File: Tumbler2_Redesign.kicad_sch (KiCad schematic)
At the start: 4 parts

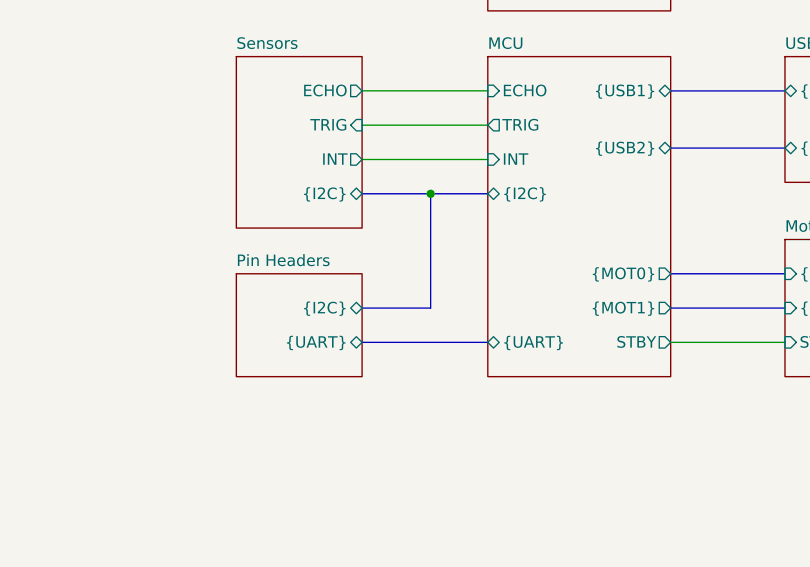
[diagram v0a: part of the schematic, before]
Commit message: Add expansion pin headers
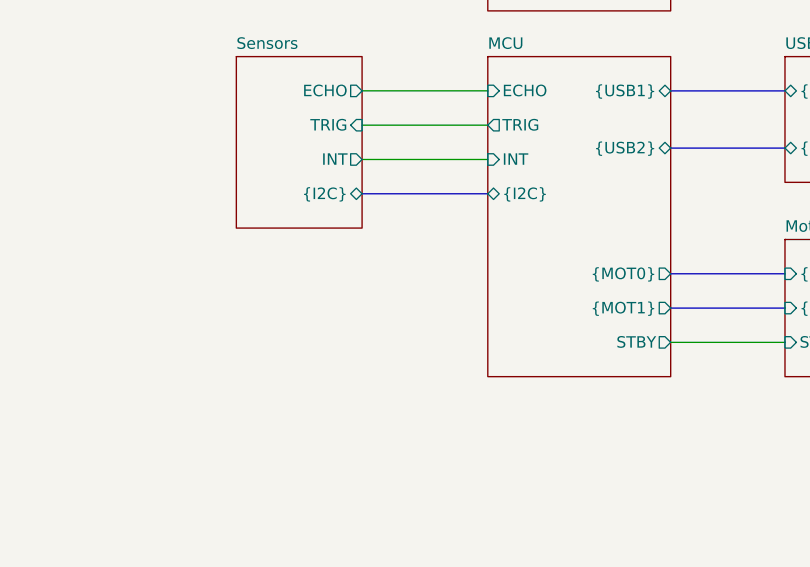
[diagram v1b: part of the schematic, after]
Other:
- removed sheet Pin Headers
- sheet MCU ports: added none; removed {UART}
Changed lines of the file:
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@@
 		)
-	)
-	(junction
-		(at 127 99.06)
-		(diameter 0)
-		(color 0 0 0 0)
 	)
 	(wire
@@
 	(bus
 		(pts
-			(xy 119.38 115.57) (xy 133.35 115.57)
+			(xy 153.67 87.63) (xy 166.37 87.63)
 		)
 		(stroke
@@
 	(bus
 		(pts
-			(xy 153.67 87.63) (xy 166.37 87.63)
+			(xy 153.67 111.76) (xy 166.37 111.76)
+		)
+		(stroke
+			(width 0)
+			(type default)
+		)
+	)
+	(wire
+		(pts
+			(xy 119.38 91.44) (xy 133.35 91.44)
 		)
 		(stroke
@@
 	(bus
 		(pts
-			(xy 153.67 111.76) (xy 166.37 111.76)
+			(xy 153.67 107.95) (xy 166.37 107.95)
 		)
 		(stroke
@@
 	(wire
 		(pts
-			(xy 119.38 91.44) (xy 133.35 91.44)
+			(xy 119.38 95.25) (xy 133.35 95.25)
 		)
 		(stroke
@@
 	(bus
 		(pts
-			(xy 153.67 107.95) (xy 166.37 107.95)
+			(xy 153.67 93.98) (xy 166.37 93.98)
+		)
+		(stroke
+			(width 0)
+			(type default)
+		)
+	)
+	(wire
+		(pts
+			(xy 153.67 115.57) (xy 166.37 115.57)
 		)
 		(stroke
@@
 	(bus
 		(pts
-			(xy 127 99.06) (xy 133.35 99.06)
-		)
-		(stroke
-			(width 0)
-			(type default)
-		)
-	)
-	(wire
-		(pts
-			(xy 119.38 95.25) (xy 133.35 95.25)
-		)
-		(stroke
-			(width 0)
-			(type default)
-		)
-	)
-	(bus
-		(pts
-			(xy 153.67 93.98) (xy 166.37 93.98)
-		)
-		(stroke
-			(width 0)
-			(type default)
-		)
-	)
-	(wire
-		(pts
-			(xy 153.67 115.57) (xy 166.37 115.57)
-		)
-		(stroke
-			(width 0)
-			(type default)
-		)
-	)
-	(bus
-		(pts
-			(xy 119.38 111.76) (xy 127 111.76)
-		)
-		(stroke
-			(width 0)
-			(type default)
-		)
-	)
-	(bus
-		(pts
-			(xy 119.38 99.06) (xy 127 99.06)
-		)
-		(stroke
-			(width 0)
-			(type default)
-		)
-	)
-	(bus
-		(pts
-			(xy 127 111.76) (xy 127 99.06)
+			(xy 119.38 99.06) (xy 133.35 99.06)
 		)
 		(stroke
@@
 			)
 		)
-		(pin "{UART}" bidirectional
-			(at 133.35 115.57 180)
-			(effects
-				(font
-					(size 1.27 1.27)
-				)
-				(justify left)
-			)
-		)
 		(instances
 			(project "Tumbler2_Redesign"
@@
 				)
 			)
-		)
-	)
-	(sheet
-		(at 105.41 107.95)
-		(size 13.97 11.43)
-		(exclude_from_sim no)
-		(in_bom yes)
-		(on_board yes)
-		(dnp no)
-		(fields_autoplaced yes)
-		(stroke
-			(width 0.1524)
-			(type solid)
-		)
-		(fill
-			(color 0 0 0 0.0000)
-		)
-		(property "Sheetname" "Pin Headers"
-			(at 105.41 107.2384 0)
-			(effects
-				(font
-					(size 1.27 1.27)
-				)
-				(justify left bottom)
-			)
-		)
-		(property "Sheetfile" "pin_headers.kicad_sch"
-			(at 105.41 119.9646 0)
-			(effects
-				(font
-					(size 1.27 1.27)
-				)
-				(justify left top)
-				(hide yes)
-			)
-		)
-		(pin "{I2C}" bidirectional
-			(at 119.38 111.76 0)
-			(effects
-				(font
-					(size 1.27 1.27)
-				)
-				(justify right)
-			)
-		)
-		(pin "{UART}" bidirectional
-			(at 119.38 115.57 0)
-			(effects
-				(font
-					(size 1.27 1.27)
-				)
-				(justify right)
-			)
-		)
-		(instances
-			(project "Tumbler2_Redesign"
-				(path "/f3fd8d79-9d35-4c04-811e-2697a2740958"
-					(page "7")
-				)
-			)

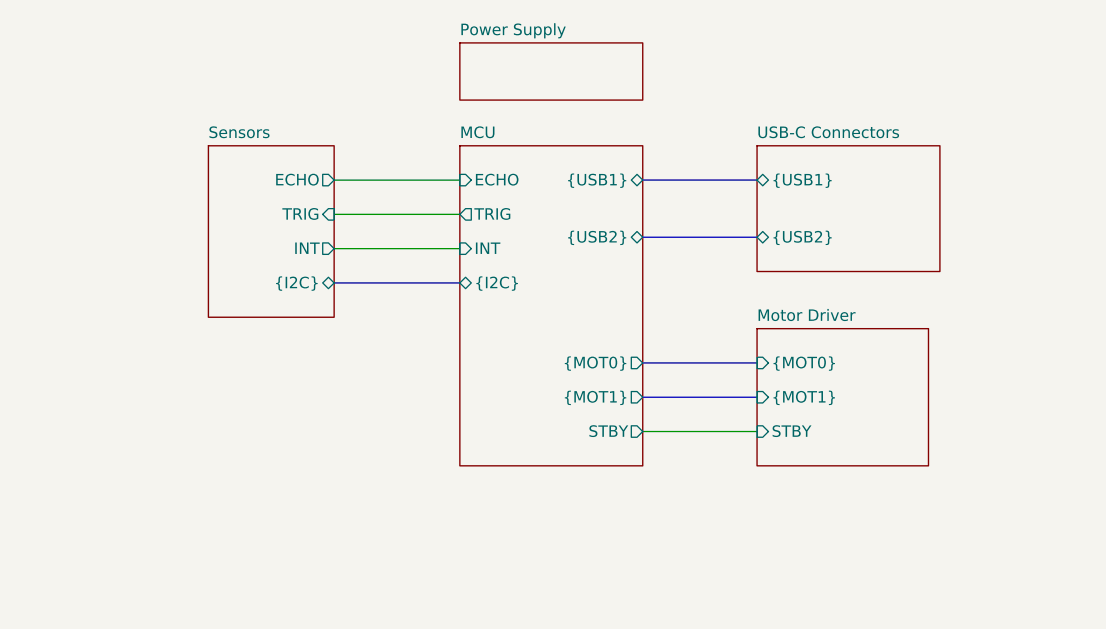
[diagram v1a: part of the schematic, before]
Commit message: Combine peripheral modules
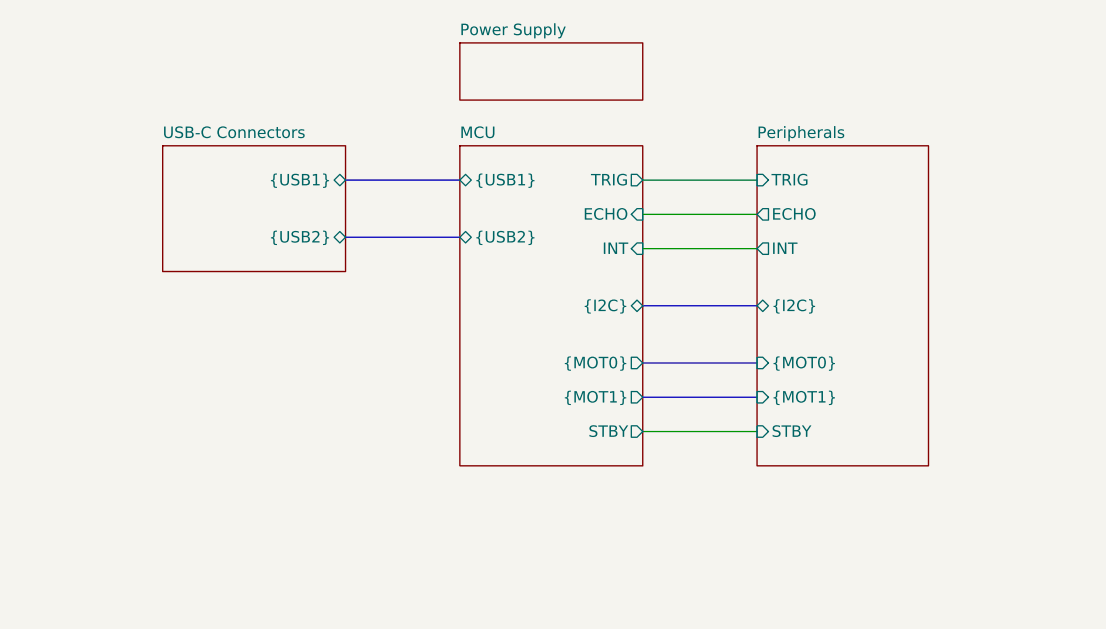
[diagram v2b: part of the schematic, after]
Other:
- removed sheet Motor Driver
- removed sheet Sensors
- added sheet Peripherals (peripherals.kicad_sch)
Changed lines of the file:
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@@
-		)
-	)
-	(wire
-		(pts
-			(xy 119.38 87.63) (xy 133.35 87.63)
-		)
-		(stroke
-			(width 0)
-			(type default)
-		)
-	)
-	(bus
-		(pts
-			(xy 153.67 87.63) (xy 166.37 87.63)
-		)
-		(stroke
-			(width 0)
-			(type default)
 		)
 	)
@@
 	(wire
 		(pts
-			(xy 119.38 91.44) (xy 133.35 91.44)
+			(xy 153.67 87.63) (xy 166.37 87.63)
 		)
 		(stroke
@@
 	(wire
 		(pts
-			(xy 119.38 95.25) (xy 133.35 95.25)
-		)
-		(stroke
-			(width 0)
-			(type default)
-		)
-	)
-	(bus
-		(pts
-			(xy 153.67 93.98) (xy 166.37 93.98)
+			(xy 153.67 95.25) (xy 166.37 95.25)
 		)
 		(stroke
@@
 		)
 	)
+	(wire
+		(pts
+			(xy 153.67 91.44) (xy 166.37 91.44)
+		)
+		(stroke
+			(width 0)
+			(type default)
+		)
+	)
 	(bus
 		(pts
-			(xy 119.38 99.06) (xy 133.35 99.06)
+			(xy 153.67 101.6) (xy 166.37 101.6)
+		)
+		(stroke
+			(width 0)
+			(type default)
+		)
+	)
+	(bus
+		(pts
+			(xy 120.65 93.98) (xy 133.35 93.98)
+		)
+		(stroke
+			(width 0)
+			(type default)
+		)
+	)
+	(bus
+		(pts
+			(xy 120.65 87.63) (xy 133.35 87.63)
 		)
 		(stroke
@@
 			)
 		)
+		(pin "{USB1}" bidirectional
+			(at 133.35 87.63 180)
+			(effects
+				(font
+					(size 1.27 1.27)
+				)
+				(justify left)
+			)
+		)
+		(pin "{USB2}" bidirectional
+			(at 133.35 93.98 180)
+			(effects
+				(font
+					(size 1.27 1.27)
+				)
+				(justify left)
+			)
+		)
 		(pin "ECHO" input
-			(at 133.35 87.63 180)
-			(effects
-				(font
-					(size 1.27 1.27)
-				)
-				(justify left)
+			(at 153.67 91.44 0)
+			(effects
+				(font
+					(size 1.27 1.27)
+				)
+				(justify right)
 			)
 		)
 		(pin "INT" input
-			(at 133.35 95.25 180)
-			(effects
-				(font
-					(size 1.27 1.27)
-				)
-				(justify left)
+			(at 153.67 95.25 0)
+			(effects
+				(font
+					(size 1.27 1.27)
+				)
+				(justify right)
 			)
 		)
 		(pin "TRIG" output
-			(at 133.35 91.44 180)
-			(effects
-				(font
-					(size 1.27 1.27)
-				)
-				(justify left)
-			)
-		)
-		(pin "{USB1}" bidirectional
 			(at 153.67 87.63 0)
 			(effects
@@
 			)
 		)
-		(pin "{USB2}" bidirectional
-			(at 153.67 93.98 0)
+		(pin "{I2C}" bidirectional
+			(at 153.67 101.6 0)
 			(effects
 				(font
@@
 			)
 		)
-		(pin "{I2C}" bidirectional
-			(at 133.35 99.06 180)
-			(effects
-				(font
-					(size 1.27 1.27)
-				)
-				(justify left)
-			)
-		)
 		(instances
 			(project "Tumbler2_Redesign"
@@
 	)
 	(sheet
-		(at 105.41 83.82)
-		(size 13.97 19.05)
+		(at 100.33 83.82)
+		(size 20.32 13.97)
 		(exclude_from_sim no)
 		(in_bom yes)
@@
 			(color 0 0 0 0.0000)
 		)
-		(property "Sheetname" "Sensors"
-			(at 105.41 83.1084 0)
+		(property "Sheetname" "USB-C Connectors"
+			(at 100.33 83.1084 0)
 			(effects
 				(font
@@
 			)
 		)
-		(property "Sheetfile" "sensors.kicad_sch"
-			(at 105.41 103.4546 0)
+		(property "Sheetfile" "usb_c_connector.kicad_sch"
+			(at 100.33 98.3746 0)
 			(effects
 				(font
@@
 			)
 		)
-		(pin "ECHO" output
-			(at 119.38 87.63 0)
+		(pin "{USB1}" bidirectional
+			(at 120.65 87.63 0)
 			(effects
 				(font
@@
 			)
 		)
-		(pin "INT" output
-			(at 119.38 95.25 0)
+		(pin "{USB2}" bidirectional
+			(at 120.65 93.98 0)
 			(effects
 				(font
@@
 			)
 		)
-		(pin "TRIG" input
-			(at 119.38 91.44 0)
-			(effects
-				(font
-					(size 1.27 1.27)
-				)
-				(justify right)
-			)
-		)
-		(pin "{I2C}" bidirectional
-			(at 119.38 99.06 0)
-			(effects
-				(font
-					(size 1.27 1.27)
-				)
-				(justify right)
-			)
-		)
 		(instances
 			(project "Tumbler2_Redesign"
 				(path "/f3fd8d79-9d35-4c04-811e-2697a2740958"
-					(page "5")
+					(page "4")
 				)
 			)
@@
 	(sheet
 		(at 166.37 83.82)
-		(size 20.32 13.97)
+		(size 19.05 35.56)
 		(exclude_from_sim no)
 		(in_bom yes)
@@
 			(color 0 0 0 0.0000)
 		)
-		(property "Sheetname" "USB-C Connectors"
+		(property "Sheetname" "Peripherals"
 			(at 166.37 83.1084 0)
 			(effects
@@
 			)
 		)
-		(property "Sheetfile" "usb_c_connector.kicad_sch"
-			(at 166.37 98.3746 0)
+		(property "Sheetfile" "peripherals.kicad_sch"
+			(at 166.37 119.9646 0)
 			(effects
 				(font
@@
 			)
 		)
-		(pin "{USB1}" bidirectional
+		(pin "ECHO" output
+			(at 166.37 91.44 180)
+			(effects
+				(font
+					(size 1.27 1.27)
+				)
+				(justify left)
+			)
+		)
+		(pin "INT" output
+			(at 166.37 95.25 180)
+			(effects
+				(font
+					(size 1.27 1.27)
+				)
+				(justify left)
+			)
+		)
+		(pin "STBY" input
+			(at 166.37 115.57 180)
+			(effects
+				(font
+					(size 1.27 1.27)
+				)
+				(justify left)
+			)
+		)
+		(pin "TRIG" input
 			(at 166.37 87.63 180)
 			(effects
@@
 			)
 		)
-		(pin "{USB2}" bidirectional
-			(at 166.37 93.98 180)
-			(effects
-				(font
-					(size 1.27 1.27)
-				)
-				(justify left)
-			)
-		)
-		(instances
-			(project "Tumbler2_Redesign"
-				(path "/f3fd8d79-9d35-4c04-811e-2697a2740958"
-					(page "4")
-				)
-			)
-		)
-	)
-	(sheet
-		(at 166.37 104.14)
-		(size 19.05 15.24)
-		(exclude_from_sim no)
-		(in_bom yes)
-		(on_board yes)
-		(dnp no)
-		(fields_autoplaced yes)
-		(stroke
-			(width 0.1524)
-			(type solid)
-		)
-		(fill
-			(color 0 0 0 0.0000)
-		)
-		(property "Sheetname" "Motor Driver"
-			(at 166.37 103.4284 0)
-			(effects
-				(font
-					(size 1.27 1.27)
-				)
-				(justify left bottom)
-			)
-		)
-		(property "Sheetfile" "motor_driver.kicad_sch"
-			(at 166.37 119.9646 0)
-			(effects
-				(font
-					(size 1.27 1.27)
-				)
-				(justify left top)
-				(hide yes)
+		(pin "{I2C}" bidirectional
+			(at 166.37 101.6 180)
+			(effects
+				(font
+					(size 1.27 1.27)
+				)
+				(justify left)
 			)
 		)
@@
 			)
 		)
-		(pin "STBY" input
-			(at 166.37 115.57 180)
-			(effects
-				(font
-					(size 1.27 1.27)
-				)
-				(justify left)
-			)
-		)
 		(instances
 			(project "Tumbler2_Redesign"
 				(path "/f3fd8d79-9d35-4c04-811e-2697a2740958"
-					(page "6")
-				)
-			)
+					(page "5")
+				)
+			)

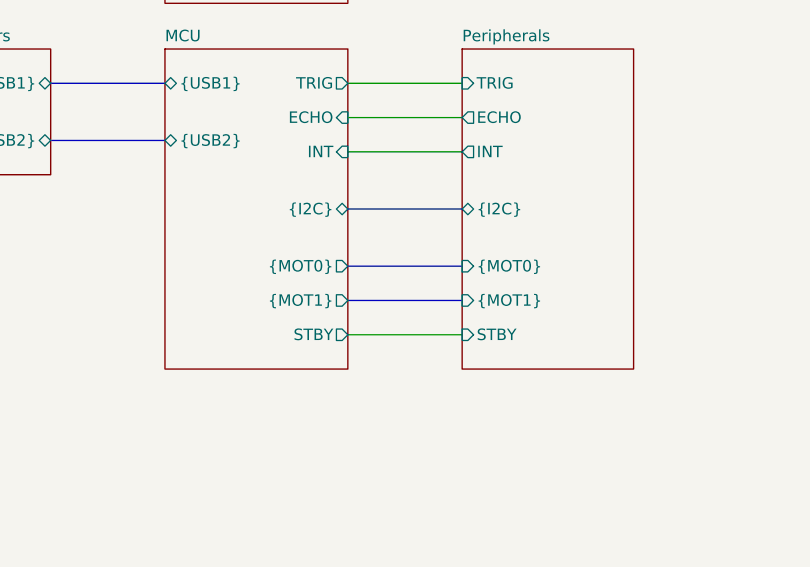
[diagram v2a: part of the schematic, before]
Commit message: Correct voltage level translation
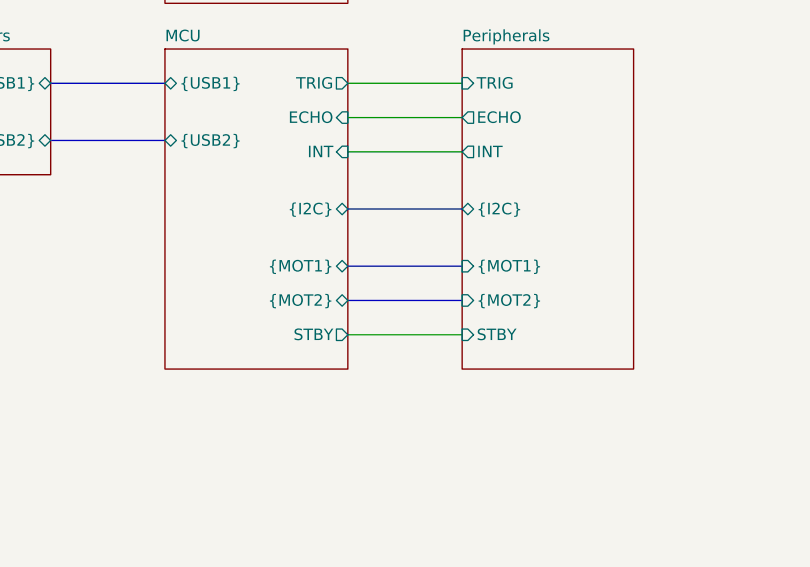
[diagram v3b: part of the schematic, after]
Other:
- sheet MCU ports: added {MOT2}; removed {MOT0}
- sheet Peripherals ports: added {MOT2}; removed {MOT0}
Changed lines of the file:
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@@
-			)
-		)
-		(pin "{MOT0}" output
-			(at 153.67 107.95 0)
-			(effects
-				(font
-					(size 1.27 1.27)
-				)
-				(justify right)
-			)
-		)
-		(pin "{MOT1}" output
-			(at 153.67 111.76 0)
-			(effects
-				(font
-					(size 1.27 1.27)
-				)
-				(justify right)
 			)
 		)
@@
 		(pin "{I2C}" bidirectional
 			(at 153.67 101.6 0)
+			(effects
+				(font
+					(size 1.27 1.27)
+				)
+				(justify right)
+			)
+		)
+		(pin "{MOT1}" bidirectional
+			(at 153.67 107.95 0)
+			(effects
+				(font
+					(size 1.27 1.27)
+				)
+				(justify right)
+			)
+		)
+		(pin "{MOT2}" bidirectional
+			(at 153.67 111.76 0)
 			(effects
 				(font
@@
 			)
 		)
-		(pin "{MOT0}" input
+		(pin "{MOT1}" input
 			(at 166.37 107.95 180)
 			(effects
@@
 			)
 		)
-		(pin "{MOT1}" input
+		(pin "{MOT2}" input
 			(at 166.37 111.76 180)
 			(effects

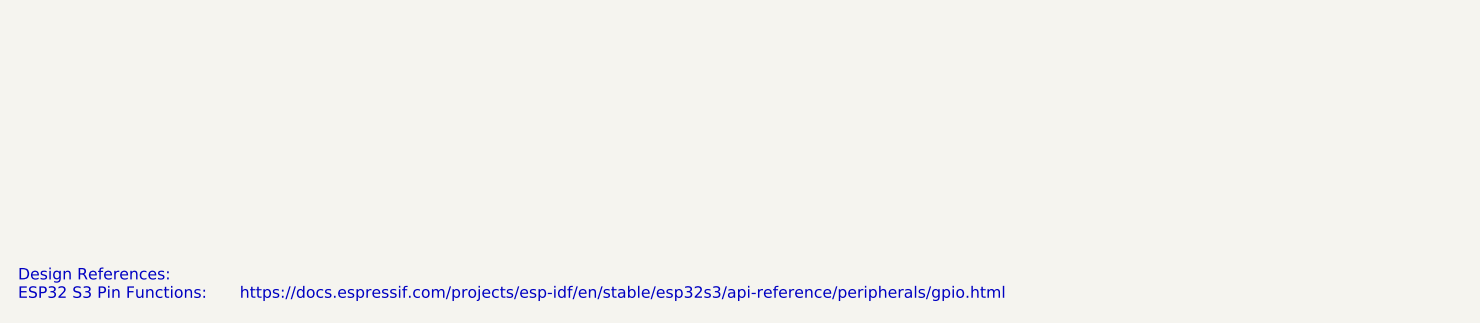
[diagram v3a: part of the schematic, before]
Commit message: Break out ADC and touch pins
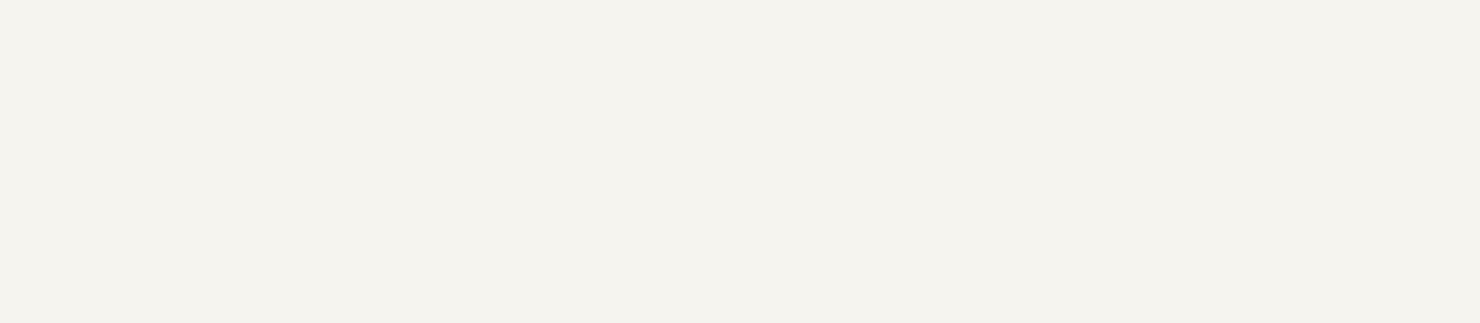
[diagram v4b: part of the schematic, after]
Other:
- note removed: "Design References: ESP32 S3 Pin Functions:"
- note removed: "https://docs.espressif.com/projects/esp-idf/en/stable/esp32s3/api-reference/peripherals/gpio.html"
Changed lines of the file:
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@@
 		(members "DP" "DM")
-	)
-	(text "https://docs.espressif.com/projects/esp-idf/en/stable/esp32s3/api-reference/peripherals/gpio.html"
-		(exclude_from_sim no)
-		(at 43.688 189.484 0)
-		(effects
-			(font
-				(size 1.27 1.27)
-			)
-			(justify left)
-			(href "https://docs.espressif.com/projects/esp-idf/en/stable/esp32s3/api-reference/peripherals/gpio.html")
-		)
-	)
-	(text "Design References:\nESP32 S3 Pin Functions: "
-		(exclude_from_sim no)
-		(at 19.05 188.468 0)
-		(effects
-			(font
-				(size 1.27 1.27)
-			)
-			(justify left)
-		)
 	)
 	(bus
